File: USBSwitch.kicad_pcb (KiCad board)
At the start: 2 copper layers, 17.8 x 17.2 mm, 5 parts, among them J1 USB_B_Micro, J2 USB_B_Micro, J3 Conn_01x02_Pin

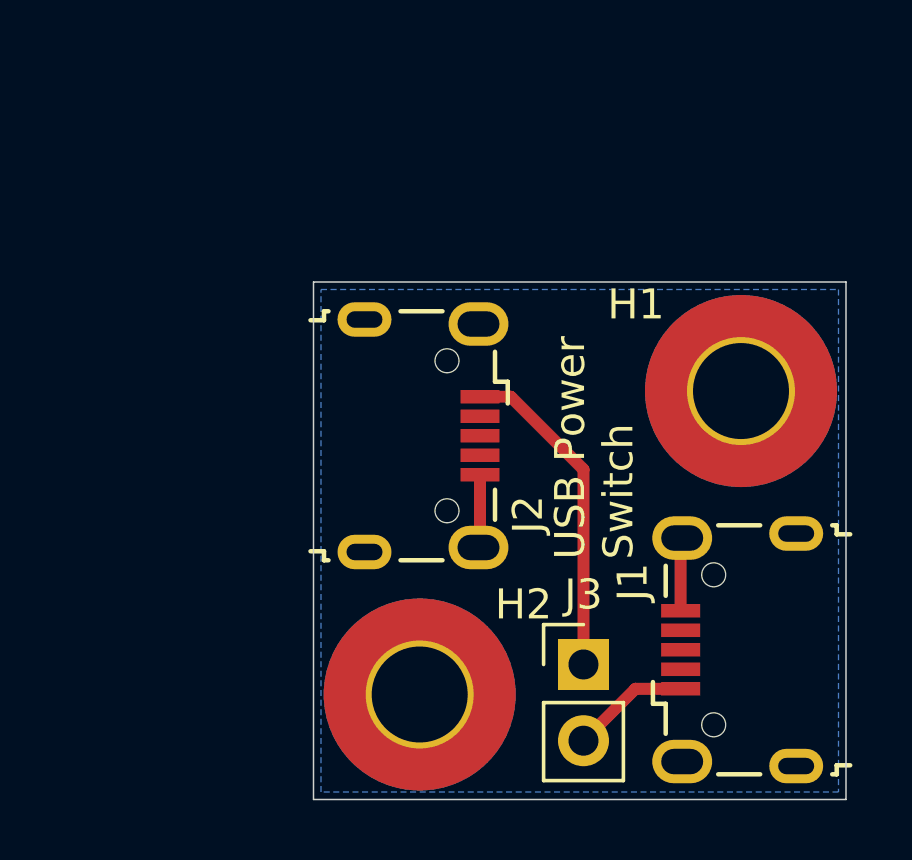
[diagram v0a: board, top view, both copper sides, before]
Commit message: Replace one micro-USB with USB-A
It's surprisingly hard to find micro-USB to micro-USB cables that can
handle full USB 2.0 current, so replace one of the connectors with a
USB-A since USB-A to micro-USB cables are plentiful
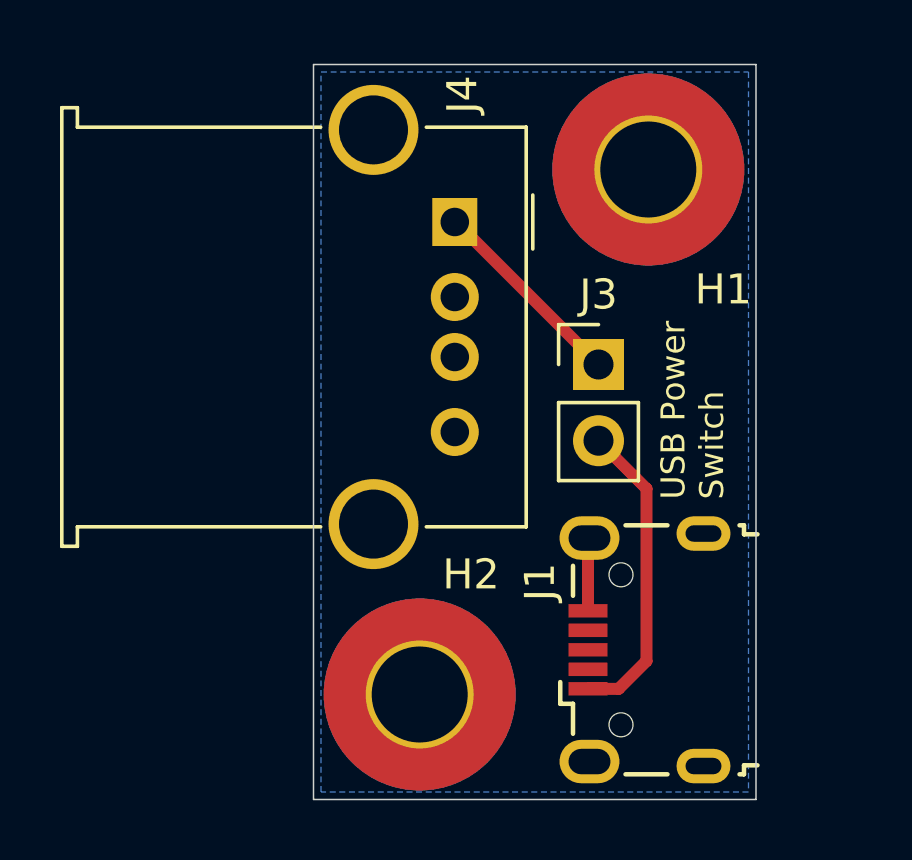
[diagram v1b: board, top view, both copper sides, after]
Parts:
- removed J2: USB_B_Micro, Connector_USB:USB_Micro-B_Wuerth_629105150521
- added J4: USB_A, Connector_USB:USB_A_Molex_67643_Horizontal, F.Cu at (146.2, 81.0)
- moved J3 10.0 mm to (151.0, 85.8)
- moved H1 8.01 mm to (152.7, 79.2)
- moved J1 3.09 mm to (152.6, 95.3)
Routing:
- net /VBUSB: track 3.96 -> 10.3 mm
- net /VBUSA: track 11.0 -> 6.76 mm
- net GNDREF: track 4.89 -> 2.45 mm
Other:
- board size 17.8 x 17.2 mm -> 14.8 x 24.5 mm
